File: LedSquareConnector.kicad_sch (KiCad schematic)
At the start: 10 parts, among them J101 Conn_02x05_Odd_Even, J102 Conn_02x05_Odd_Even, J103 Conn_02x05_Odd_Even, J104 Conn_02x05_Odd_Even

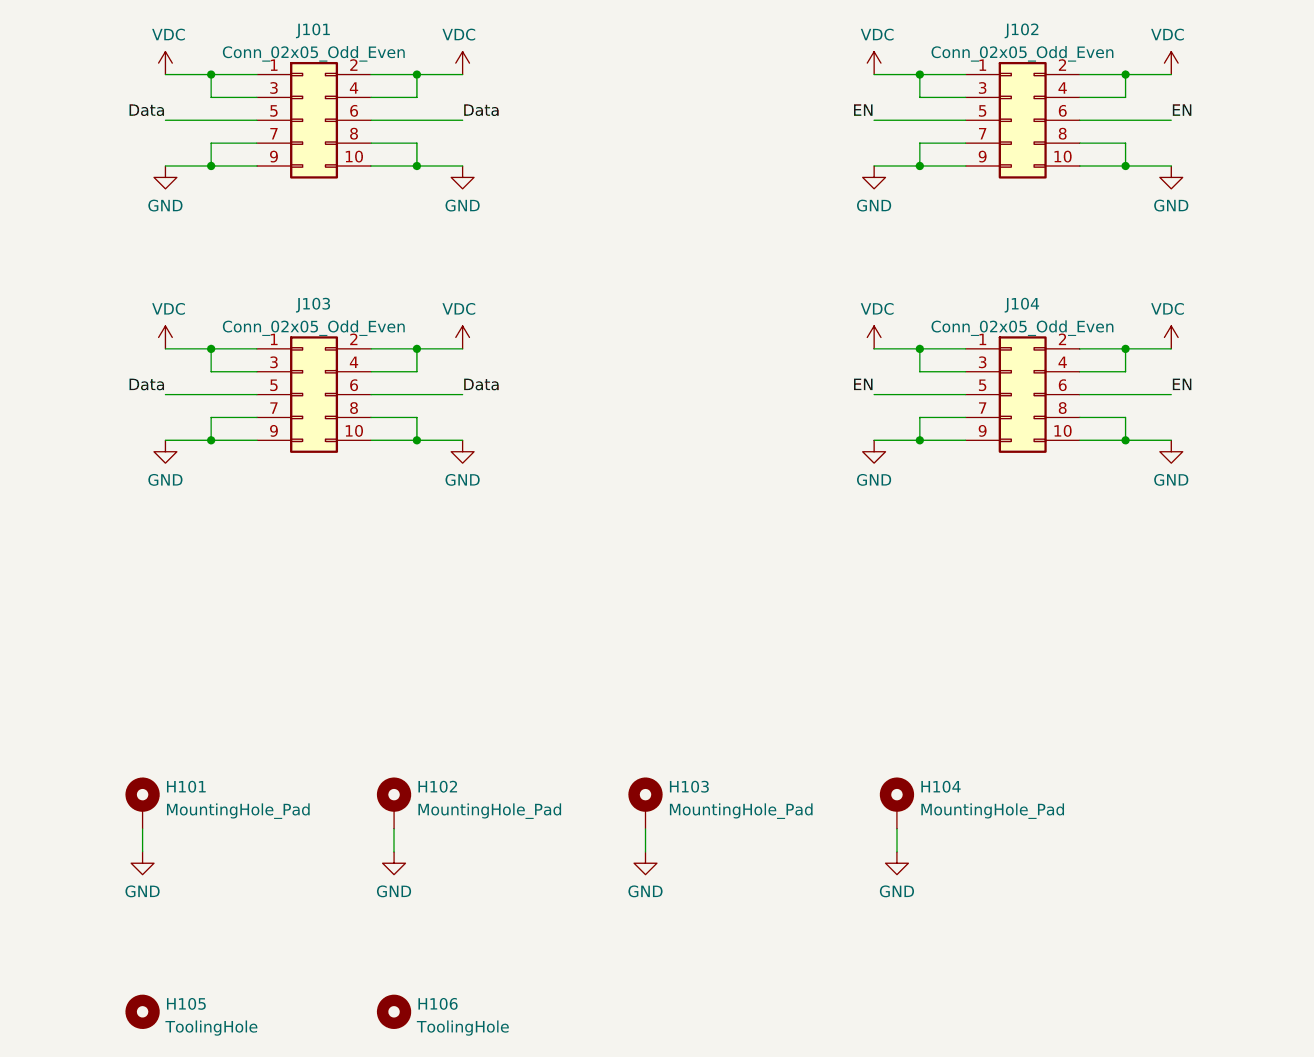
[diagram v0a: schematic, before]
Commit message: Change connector and prep for manufactoring
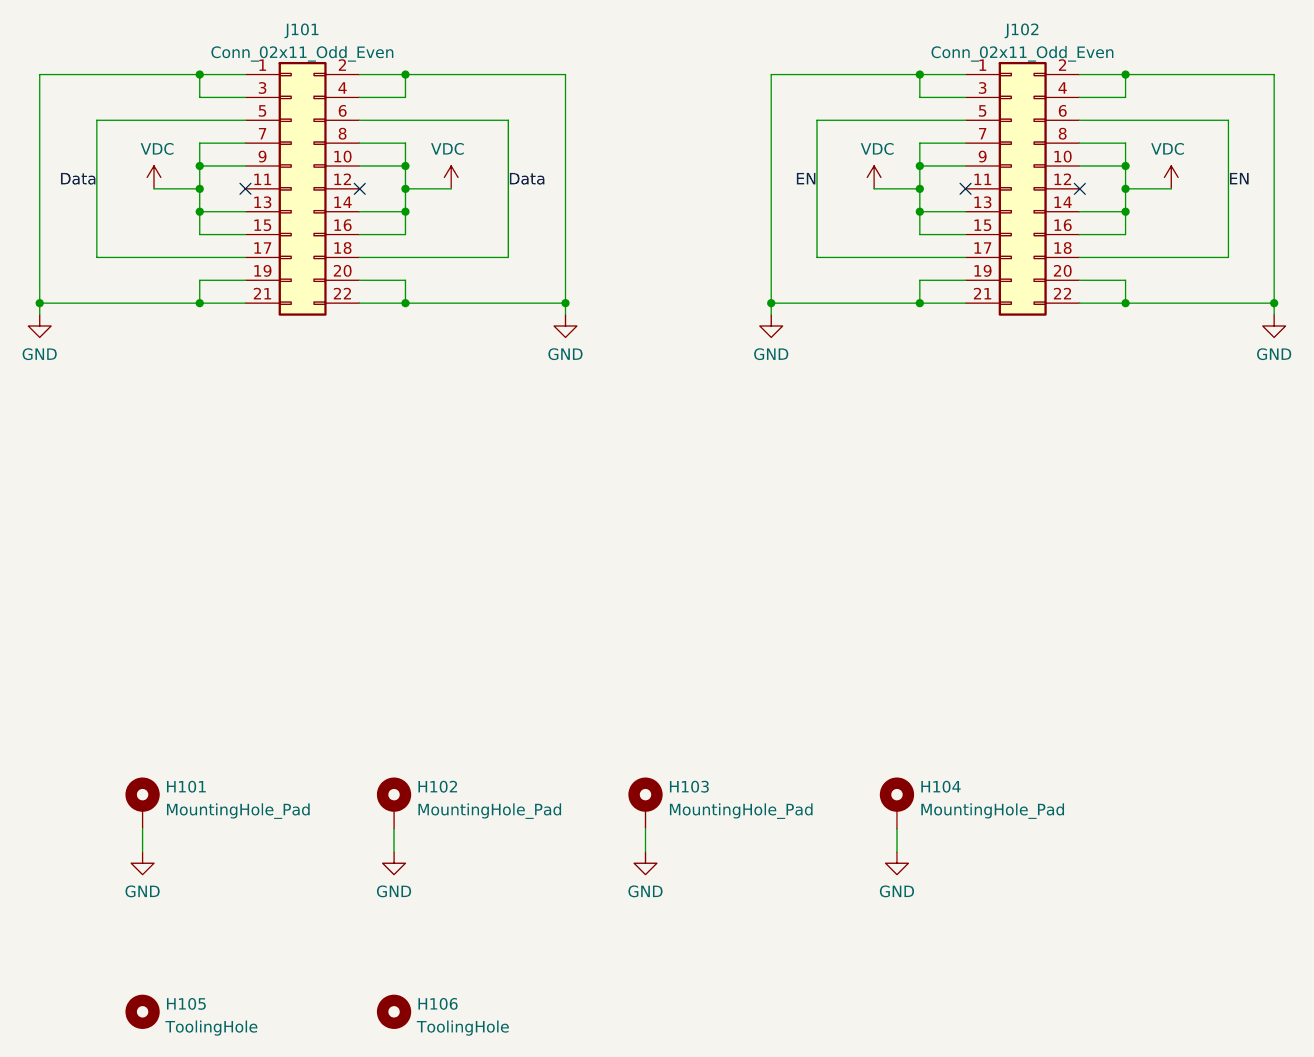
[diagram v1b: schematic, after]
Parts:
- removed J101, J102, J103, J104: Conn_02x05_Odd_Even, Connector_PinSocket_2.54mm:PinSocket_2x05_P2.54mm_Vertical, symbol Connector_Generic:Conn_02x05_Odd_Even
- added J101, J102: Conn_02x11_Odd_Even, Connector_PinSocket_2.54mm:PinSocket_2x11_P2.54mm_Vertical, symbol Connector_Generic:Conn_02x11_Odd_Even
- H101, H102, H103, H104: footprint MountingHole:MountingHole_5.3mm_M5_ISO7380_Pad_TopBottom -> MountingHole:MountingHole_5.3mm_M5_Pad_Via
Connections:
- net Data: now also J101.17 (Pin_17), J101.18 (Pin_18), J101.5 (Pin_5), J101.6 (Pin_6)
- net EN: now also J102.17 (Pin_17), J102.18 (Pin_18), J102.5 (Pin_5), J102.6 (Pin_6)
- net GND: now also J101.1 (Pin_1), J101.19 (Pin_19), J101.2 (Pin_2), J101.20 (Pin_20), J101.21 (Pin_21), J101.22 (Pin_22), J101.3 (Pin_3), J101.4 (Pin_4), J102.1 (Pin_1), J102.19 (Pin_19), J102.2 (Pin_2), J102.20 (Pin_20), J102.21 (Pin_21), J102.22 (Pin_22), J102.3 (Pin_3), J102.4 (Pin_4)
- net VDC: now also J101.10 (Pin_10), J101.13 (Pin_13), J101.14 (Pin_14), J101.15 (Pin_15), J101.16 (Pin_16), J101.7 (Pin_7), J101.8 (Pin_8), J101.9 (Pin_9), J102.10 (Pin_10), J102.13 (Pin_13), J102.14 (Pin_14), J102.15 (Pin_15), J102.16 (Pin_16), J102.7 (Pin_7), J102.8 (Pin_8), J102.9 (Pin_9)
- no-connect marks 0 -> 4

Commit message: Add LCSC partnumbers to headers
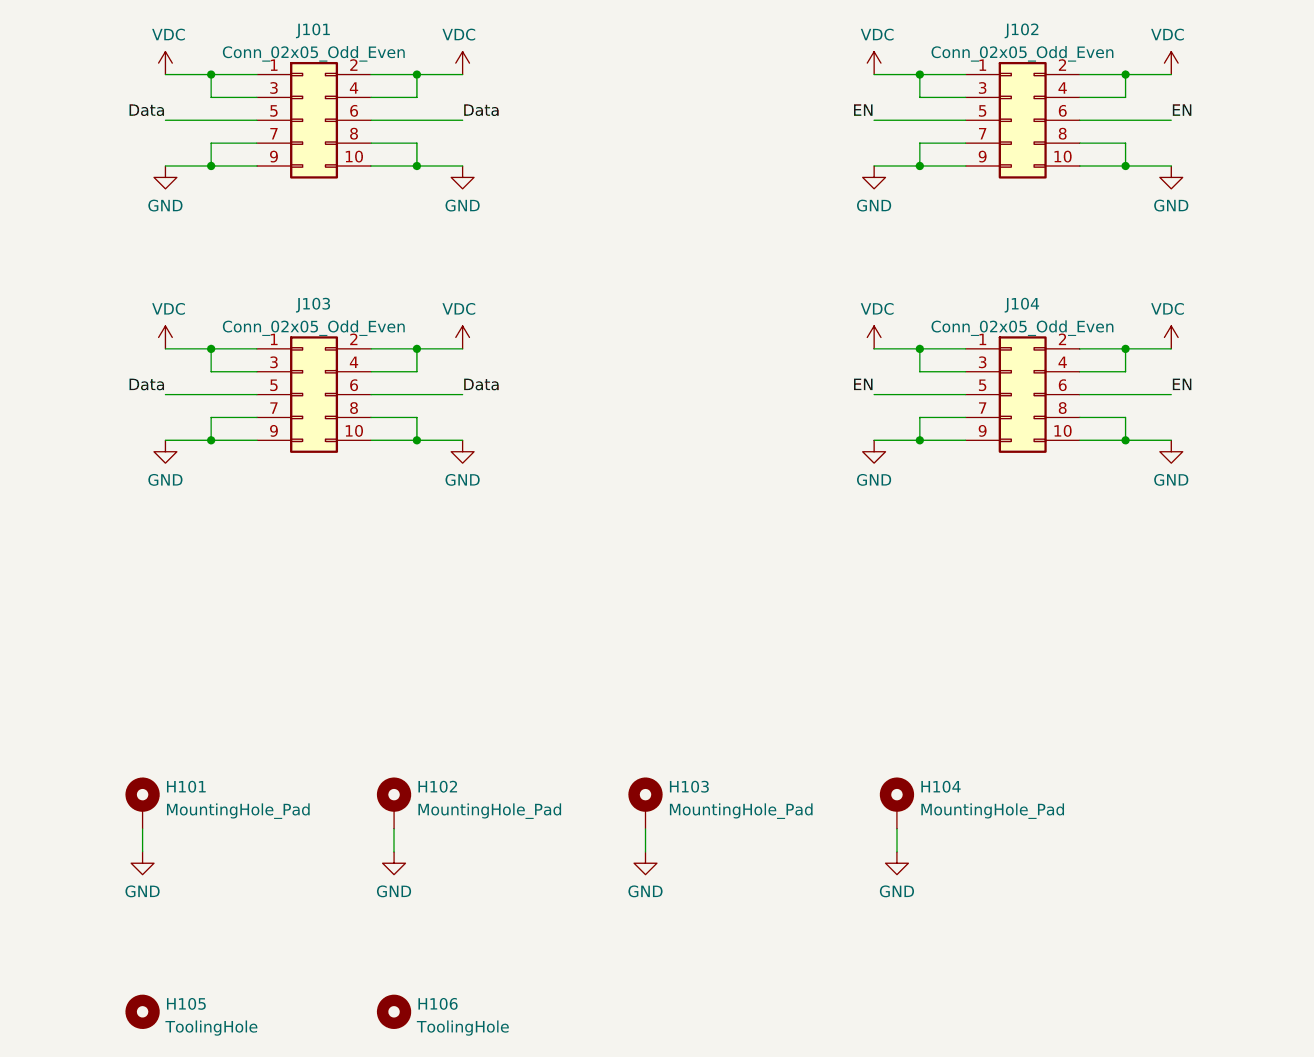
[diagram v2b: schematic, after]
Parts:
- removed J101, J102: Conn_02x11_Odd_Even, Connector_PinSocket_2.54mm:PinSocket_2x11_P2.54mm_Vertical, symbol Connector_Generic:Conn_02x11_Odd_Even
- added J101, J102, J103, J104: Conn_02x05_Odd_Even, Connector_PinHeader_2.54mm:PinHeader_2x05_P2.54mm_Vertical, symbol Connector_Generic:Conn_02x05_Odd_Even
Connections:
- net Data: now also J101.5 (Pin_5), J101.6 (Pin_6), J103.5 (Pin_5), J103.6 (Pin_6)
- net EN: now also J102.5 (Pin_5), J102.6 (Pin_6), J104.5 (Pin_5), J104.6 (Pin_6)
- net GND: now also J101.10 (Pin_10), J101.7 (Pin_7), J101.8 (Pin_8), J101.9 (Pin_9), J102.10 (Pin_10), J102.7 (Pin_7), J102.8 (Pin_8), J102.9 (Pin_9), J103.10 (Pin_10), J103.7 (Pin_7), J103.8 (Pin_8), J103.9 (Pin_9), J104.10 (Pin_10), J104.7 (Pin_7), J104.8 (Pin_8), J104.9 (Pin_9)
- net VDC: now also J101.1 (Pin_1), J101.2 (Pin_2), J101.3 (Pin_3), J101.4 (Pin_4), J102.1 (Pin_1), J102.2 (Pin_2), J102.3 (Pin_3), J102.4 (Pin_4), J103.1 (Pin_1), J103.2 (Pin_2), J103.3 (Pin_3), J103.4 (Pin_4), J104.1 (Pin_1), J104.2 (Pin_2), J104.3 (Pin_3), J104.4 (Pin_4)
- no-connect marks 4 -> 0
